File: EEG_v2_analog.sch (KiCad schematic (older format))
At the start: 51 parts, among them J1 BIAS, U1 ADS1299IPAGR

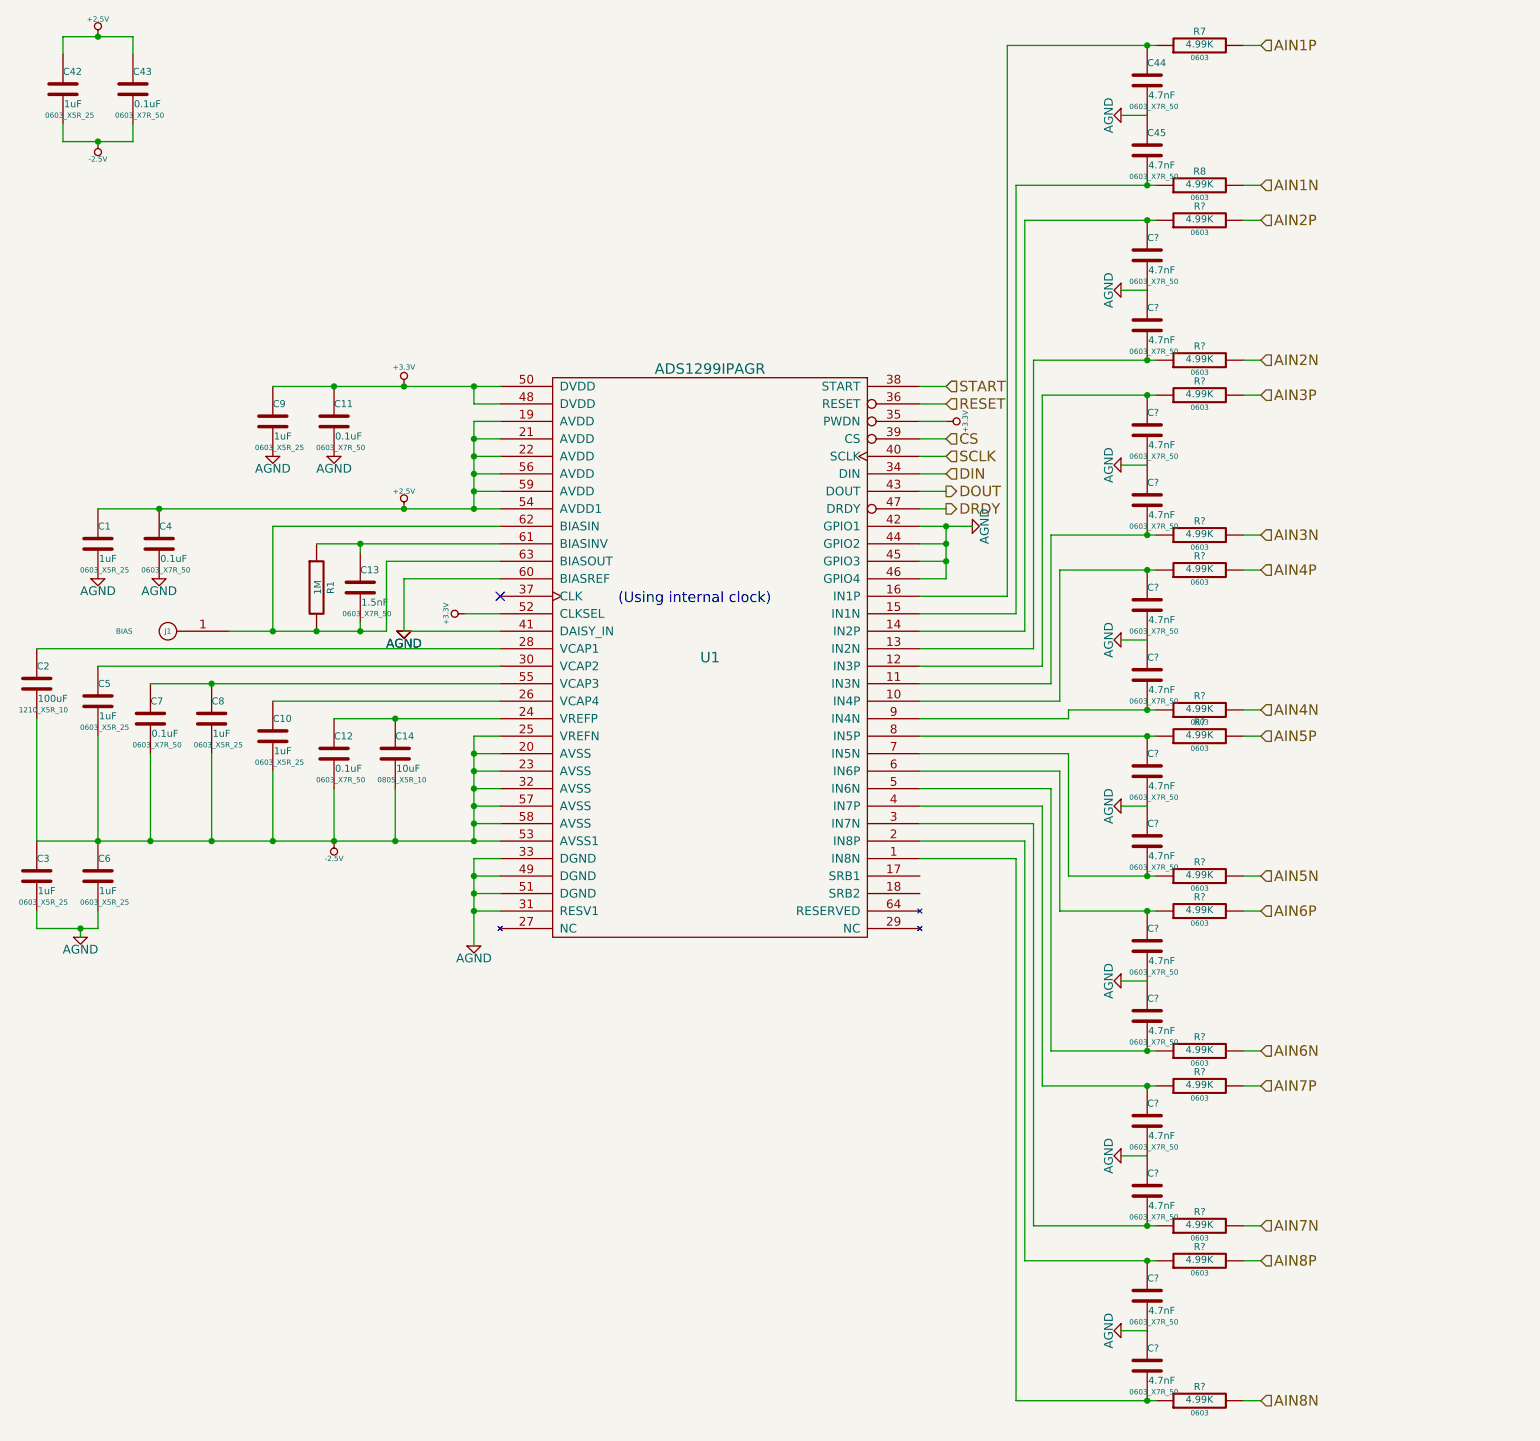
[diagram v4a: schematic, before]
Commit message: Added pins for bias and SRB1/2
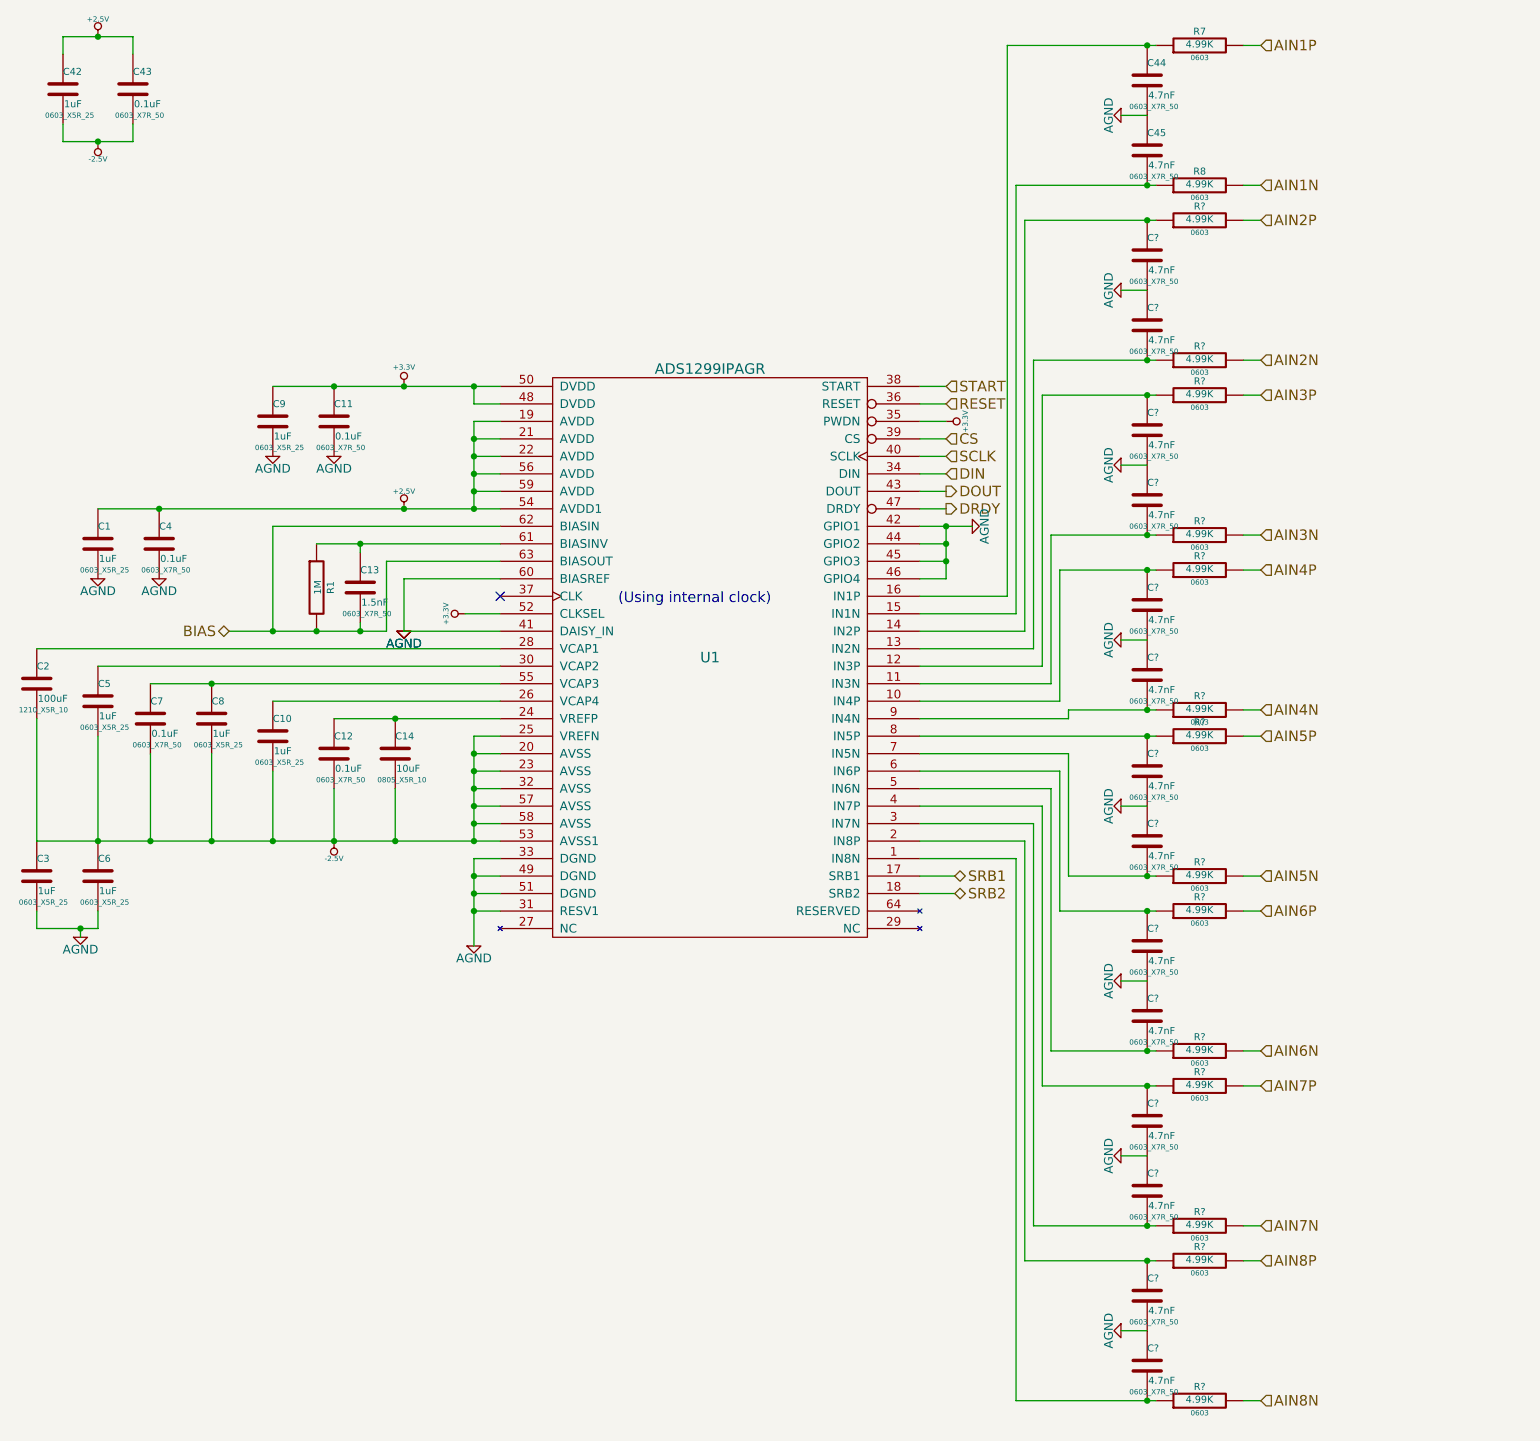
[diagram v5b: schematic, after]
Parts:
- removed J1: BIAS, ~, symbol SMD_1PIN_PAD
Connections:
- net SRB1: now reaches U1.17 (SRB1)
- net SRB2: now reaches U1.18 (SRB2)
- net BIAS: now reaches C13.2, R1.2, U1.62 (BIASIN), U1.63 (BIASOUT)
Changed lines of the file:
@@
 $EndComp
 Wire Wire Line
-	2000 2750 2350 2750
-Wire Wire Line
-	2350 2750 2750 2750
-Wire Wire Line
-	2750 2750 3150 2750
-Wire Wire Line
-	3150 2750 3300 2750
+	2000 2750 3300 2750
 Wire Wire Line
 	3300 2850 3150 2850
@@
 	3300 2950 3150 2950
 Wire Wire Line
-	3150 2950 3150 3050
-Wire Wire Line
-	3150 3050 3150 3150
-Wire Wire Line
-	3150 3150 3150 3250
-Wire Wire Line
-	3150 3250 3150 3350
-Wire Wire Line
-	3150 3350 3150 3450
+	3150 2950 3150 3450
 Wire Wire Line
 	3300 3350 3150 3350
@@
 	3300 5450 3150 5450
 Wire Wire Line
-	3150 5450 3150 5550
-Wire Wire Line
-	3150 5550 3150 5650
-Wire Wire Line
-	3150 5650 3150 5750
-Wire Wire Line
-	3150 5750 3150 5950
+	3150 5450 3150 5950
 Wire Wire Line
 	3150 5550 3300 5550
@@
 Connection ~ 3150 5750
 Wire Wire Line
-	3150 5350 3150 5250
-Wire Wire Line
-	3150 5250 3150 5150
-Wire Wire Line
-	3150 5150 3150 5050
-Wire Wire Line
-	3150 5050 3150 4950
-Wire Wire Line
-	3150 4950 3150 4850
-Wire Wire Line
-	3150 4850 3150 4750
+	3150 5350 3150 4750
 Connection ~ 3150 4850
 Connection ~ 3150 4950
@@
 	3150 4850 3300 4850
 Wire Wire Line
-	650  5350 1000 5350
-Wire Wire Line
-	1000 5350 1300 5350
-Wire Wire Line
-	1300 5350 1650 5350
-Wire Wire Line
-	1650 5350 2000 5350
-Wire Wire Line
-	2000 5350 2350 5350
-Wire Wire Line
-	2350 5350 2700 5350
-Wire Wire Line
-	2700 5350 3150 5350
-Wire Wire Line
-	3150 5350 3300 5350
+	650  5350 3300 5350
 Wire Wire Line
 	650  5350 650  4650
@@
 	2000 4550 3300 4550
 Wire Wire Line
-	1300 4450 1650 4450
-Wire Wire Line
-	1650 4450 3300 4450
+	1300 4450 3300 4450
 Connection ~ 1650 4450
 Wire Wire Line
@@
 	3150 4750 3300 4750
 Wire Wire Line
-	2350 4650 2700 4650
-Wire Wire Line
-	2700 4650 3300 4650
+	2350 4650 3300 4650
 Connection ~ 2700 4650
 Wire Wire Line
@@
 	2650 3750 2650 4150
 Wire Wire Line
-	2650 4150 2500 4150
-Wire Wire Line
-	2500 4150 2250 4150
-Wire Wire Line
-	2250 4150 2000 4150
-Wire Wire Line
-	2000 4150 1750 4150
-Wire Wire Line
-	2250 3650 2500 3650
-Wire Wire Line
-	2500 3650 3300 3650
+	2650 4150 1750 4150
+Wire Wire Line
+	2250 3650 3300 3650
 Wire Wire Line
 	2500 3650 2500 3700
@@
 Connection ~ 1350 3450
 Wire Wire Line
-	1000 3450 1350 3450
-Wire Wire Line
-	1350 3450 2750 3450
-Wire Wire Line
-	2750 3450 3150 3450
-Wire Wire Line
-	3150 3450 3300 3450
+	1000 3450 3300 3450
 Wire Wire Line
 	3300 5050 3150 5050
@@
 Wire Wire Line
 	3300 4950 3150 4950
-$Comp
-L SMD_1PIN_PAD J1
-U 1 1 54B45EA3
-P 1400 4150
-F 0 "J1" H 1400 4150 30  0000 C CNN
-F 1 "BIAS" H 1650 4150 30  0000 C CNN
-F 2 "~" H 1400 4150 60  0000 C CNN
-F 3 "~" H 1400 4150 60  0000 C CNN
-	1    1400 4150
-	-1   0    0    1
-$EndComp
 Wire Wire Line
 	5700 2750 5850 2750
@@
 	5850 3450 5700 3450
 Wire Wire Line
-	5700 3550 5850 3550
-Wire Wire Line
-	5850 3550 6000 3550
+	5700 3550 6000 3550
 Wire Wire Line
 	5700 3650 5850 3650
@@
 	650  5750 650  5850
 Wire Wire Line
-	650  5850 900  5850
-Wire Wire Line
-	900  5850 1000 5850
+	650  5850 1000 5850
 Wire Wire Line
 	900  5850 900  5900
@@
 $EndComp
 Wire Wire Line
-	5850 3550 5850 3650
-Wire Wire Line
-	5850 3650 5850 3750
-Wire Wire Line
-	5850 3750 5850 3850
+	5850 3550 5850 3850
 Connection ~ 5850 3550
 Connection ~ 5850 3650
@@
 	800  850  800  750
 Wire Wire Line
-	800  750  1000 750
-Wire Wire Line
-	1000 750  1200 750
+	800  750  1200 750
 Wire Wire Line
 	1200 750  1200 850
@@
 	1200 1350 1200 1250
 Wire Wire Line
-	800  1350 1000 1350
-Wire Wire Line
-	1000 1350 1200 1350
+	800  1350 1200 1350
 Wire Wire Line
 	800  1250 800  1350
@@
 	7650 1600 7550 1600
 Wire Wire Line
-	6200 800  7000 800
-Wire Wire Line
-	7000 800  7050 800
+	6200 800  7050 800
 Connection ~ 7000 800
 Wire Wire Line
-	6250 1600 7000 1600
-Wire Wire Line
-	7000 1600 7050 1600
+	6250 1600 7050 1600
 Connection ~ 7000 1600
 $Comp
@@
 	7650 2600 7550 2600
 Wire Wire Line
-	6300 1800 7000 1800
-Wire Wire Line
-	7000 1800 7050 1800
+	6300 1800 7050 1800
 Connection ~ 7000 1800
 Wire Wire Line
-	6350 2600 7000 2600
-Wire Wire Line
-	7000 2600 7050 2600
+	6350 2600 7050 2600
 Connection ~ 7000 2600
 $Comp
@@
 	7650 3600 7550 3600
 Wire Wire Line
-	6400 2800 7000 2800
-Wire Wire Line
-	7000 2800 7050 2800
+	6400 2800 7050 2800
 Connection ~ 7000 2800
 Wire Wire Line
-	6450 3600 7000 3600
-Wire Wire Line
-	7000 3600 7050 3600
+	6450 3600 7050 3600
 Connection ~ 7000 3600
 $Comp
@@
 	7650 4600 7550 4600
 Wire Wire Line
-	6500 3800 7000 3800
-Wire Wire Line
-	7000 3800 7050 3800
+	6500 3800 7050 3800
 Connection ~ 7000 3800
 Wire Wire Line
-	6550 4600 7000 4600
-Wire Wire Line
-	7000 4600 7050 4600
+	6550 4600 7050 4600
 Connection ~ 7000 4600
 $Comp
@@
 	7650 5550 7550 5550
 Wire Wire Line
-	5700 4750 7000 4750
-Wire Wire Line
-	7000 4750 7050 4750
+	5700 4750 7050 4750
 Connection ~ 7000 4750
 Wire Wire Line
-	6550 5550 7000 5550
-Wire Wire Line
-	7000 5550 7050 5550
+	6550 5550 7050 5550
 Connection ~ 7000 5550
 $Comp
@@
 	7650 6550 7550 6550
 Wire Wire Line
-	6500 5750 7000 5750
-Wire Wire Line
-	7000 5750 7050 5750
+	6500 5750 7050 5750
 Connection ~ 7000 5750
 Wire Wire Line
-	6450 6550 7000 6550
-Wire Wire Line
-	7000 6550 7050 6550
+	6450 6550 7050 6550
 Connection ~ 7000 6550
 $Comp
@@
 	7650 7550 7550 7550
 Wire Wire Line
-	6400 6750 7000 6750
-Wire Wire Line
-	7000 6750 7050 6750
+	6400 6750 7050 6750
 Connection ~ 7000 6750
 Wire Wire Line
-	6350 7550 7000 7550
-Wire Wire Line
-	7000 7550 7050 7550
+	6350 7550 7050 7550
 Connection ~ 7000 7550
 $Comp
@@
 	7650 8550 7550 8550
 Wire Wire Line
-	6300 7750 7000 7750
-Wire Wire Line
-	7000 7750 7050 7750
+	6300 7750 7050 7750
 Connection ~ 7000 7750
 Wire Wire Line
-	6250 8550 7000 8550
-Wire Wire Line
-	7000 8550 7050 8550
+	6250 8550 7050 8550
 Connection ~ 7000 8550
 Wire Wire Line
@@
 Wire Wire Line
 	6300 5350 5700 5350
+Text HLabel 5900 5550 2    60   BiDi ~ 0
+SRB1
+Text HLabel 5900 5650 2    60   BiDi ~ 0
+SRB2
+Wire Wire Line
+	5700 5550 5900 5550
+Wire Wire Line
+	5900 5650 5700 5650
+Text HLabel 1750 4150 0    60   BiDi ~ 0
+BIAS
 $EndSCHEMATC
